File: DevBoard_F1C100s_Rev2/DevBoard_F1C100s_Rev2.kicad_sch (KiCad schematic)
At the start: 59 parts, among them J101 USB_C_Receptacle_USB2.0_16P, J105 UART0, SW105 RESET, SW106 RESET, U101 TPS562201DDCT, U102 TPS562201DDCT, U103 TPS562201DDCT, U104 W25Q16JVSS, U105 F1C100s, Y101 24Mhz

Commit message: WIP schematic
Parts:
- removed C101, C103, C104, C105, C107, C117, C122: 22uf, Capacitor_SMD:C_0603_1608Metric_Pad1.08x0.95mm_HandSolder, symbol Device:C_Small
- removed C102, C106, C118, C120, C121, C123, C124: 0.1uf, Capacitor_SMD:C_0603_1608Metric_Pad1.08x0.95mm_HandSolder, symbol Device:C_Small
- removed F101: TLC-USMD175, symbol Device:Polyfuse_Small
- removed J101: USB_C_Receptacle_USB2.0_16P, Connector_USB:USB_C_Receptacle_HRO_TYPE-C-31-M-12, symbol Connector:USB_C_Receptacle_USB2.0_16P
- removed J105: UART0, Connector_PinHeader_1.00mm:PinHeader_1x04_P1.00mm_Vertical_SMD_Pin1Left, symbol Connector_Generic:Conn_01x04
- removed L101, L102, L103: 2.2uH, Inductor_SMD:L_APV_ANR252012, symbol Device:L_Small
- removed R101, R102, R103, R104, R111: 5.1K, Resistor_SMD:R_0603_1608Metric_Pad0.98x0.95mm_HandSolder, symbol Device:R_Small
- removed R120: 10k, Resistor_SMD:R_0603_1608Metric_Pad0.98x0.95mm_HandSolder, symbol Device:R_Small
- removed SW106: RESET, Button_Switch_SMD:SW_SPST_CK_RS282G05A3, symbol Switch:SW_Push
- removed TP103, TP106, TP107: TestPoint, TestPoint:TestPoint_Pad_D1.0mm, symbol Connector:TestPoint
- removed TP108: TestPoint, TestPoint:TestPoint_Pad_D2.0mm, symbol Connector:TestPoint
- removed U101, U102, U103: TPS562201DDCT, TPS562201DDCT:DDC0006A_N, symbol TPS562201DDCT:TPS562201DDCT
- removed U105: F1C100s, F1C100s:QFN-88_EP_10x10_Pitch0.4mm, symbol F1C100s:F1C100s
- added C? (x2): 0.1uf, Capacitor_SMD:C_0603_1608Metric_Pad1.08x0.95mm_HandSolder, symbol Device:C_Small
- added J?: Micro_SD_Card_Det1, symbol sd_card:Micro_SD_Card_Det1
- added R? (x6): 10k, Resistor_SMD:R_0603_1608Metric_Pad0.98x0.95mm_HandSolder, symbol Device:R_Small
- added SW?: FEL, Button_Switch_SMD:SW_SPST_CK_RS282G05A3, symbol Switch:SW_Push
- added U1: F1C100S, symbol F1C100s:F1C100S
- renumbered C108 to C15, C109 to C16, C110 to C17, C112 to C18, C111 to C19, C113 to C20, C119 to C21, C126 to C22, C125 to C23, C127 to C24, C114 to C25, C128 to C26, C116 to C27, C115 to C28, C129 to C29, C131 to C30, C130 to C31, C132 to C32, R107 to R7, R108 to R8, R115 to R9, SW105 to SW2, U104 to U5, Y101 to Y1
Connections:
- net GND: now also C?.2, C?.2, J?.10 (SHIELD), J?.6 (VSS), SW?.1, U1.74 (TVGND), U1.82 (AGND), U1.89 (GND)
- net HOSCI: now also U1.51 (HOSCI)
- net HOSCO: now also U1.52 (HOSCO)
- net RESET: now also U1.70 (~{RESET})
- net SPI0_CLK: now also U1.59 (PC0/SPI0_CLK/SDC1_CLK)
- net SPI0_CS: now also R?.2, SW?.2, U1.60 (PC1/SPI0_CS/SDC1_CMD)
- net SPI0_MISO: now also U1.61 (PC2/SPI0_MISO/SDC1_D0)
- net SPI0_MOSI: now also U1.62 (PC3/SPI0_MOSI/UART0_TX)
- net SVREF: now also U1.33 (SVREF)
- net USB_N: now also U1.68 (USB_DM)
- net USB_P: now also U1.69 (USB_DP)
- net 1V1 renamed 1.1V
- net 1.1V: now also U1.22 (VCC_CORE), U1.35 (VCC_CORE), U1.71 (VCC_CORE)
- net 2V6 renamed 2.6V
- net 2.6V: now also U1.30 (VCC_DRAM), U1.31 (VCC_DRAM), U1.32 (VCC_DRAM), U1.34 (VCC_DRAM), U1.36 (VCC_DRAM), U1.80 (AVCC)
- net 3V3 renamed 3.3V
- net 3.3V: now also C?.1, C?.1, J?.4 (VDD), R?.1, R?.1, R?.1, R?.1, R?.1, R?.1, U1.20 (VCC_IO), U1.4 (HPVCC), U1.5 (VCC_IO), U1.50 (VCC_IO), U1.67 (USB_VCC), U1.73 (TV_VCC)
- new net LCD_CLK: U1.26 (PD18/LCD_CLK/SPI0_CS)
- new net LCD_D0: U1.49 (PE0/CSI_HSYNC/LCD_D0)
- new net LCD_D1: U1.48 (PE1/CSI_VSYNC/LCD_D1)
- new net LCD_D10: U1.12 (PD6/LCD_D10/TWI1_SDA)
- new net LCD_D11: U1.13 (PD7/LCD_D11/DA_MCLK)
- new net LCD_D12: U1.14 (PD8/LCD_D12/DA_BCLK)
- new net LCD_D13: U1.15 (PD9/LCD_D13/DA_LRCK)
- new net LCD_D14: U1.16 (PD10/LCD_D14/DA_IN)
- new net LCD_D15: U1.17 (PD11/LCD_D15/DA_OUT)
- new net LCD_D16: U1.45 (PE4/CSI_D1/LCD_D16)
- new net LCD_D17: U1.44 (PE5/CSI_D2/LCD_D17)
- new net LCD_D18: U1.18 (PD12/LCD_D18/TWI0_SCK)
- new net LCD_D19: U1.19 (PD13/LCD_D19/UART2_TX)
- new net LCD_D2: U1.6 (PD0/LCD_D2/TWI0_SDA)
- new net LCD_D20: U1.21 (PD14/LCD_D20/UART2_RX)
- new net LCD_D21: U1.23 (PD15/LCD_D21/UART2_RTS)
- new net LCD_D22: U1.24 (PD16/LCD_D22/UART2_CTS)
- new net LCD_D23: U1.25 (PD17/LCD_D23/OWA_OUT)
- new net LCD_D3: U1.7 (PD1/LCD_D3/UART1_RTS)
- new net LCD_D4: U1.8 (PD2/LCD_D4/UART1_CTS)
- new net LCD_D5: U1.9 (PD3/LCD_D5/UART1_RX)
- new net LCD_D6: U1.10 (PD4/LCD_D6/UART1_TX)
- new net LCD_D7: U1.11 (PD5/LCD_D7/TWI1_SCK)
- new net LCD_D8: U1.47 (PE2/CSI_PCLK/LCD_D8)
- new net LCD_D9: U1.46 (PE3/CSI_D0/LCD_D9)
- new net LCD_DE: U1.27 (PD19/LCD_DE/SPI0_MOSI)
- new net LCD_HSYNC: U1.28 (PD20/LCD_HSYNC/SPI0_CLK)
- new net LCD_VSYNC: U1.29 (PD21/LCD_VSYNC/SPI0_MISO)
- new net SDC0_CLK: J?.5 (CLK), U1.56 (PF2/SDC0_CLK/UART0_RX)
- new net SDC0_CMD: J?.3 (CMD), R?.2, U1.55 (PF3/SDC0_CMD/DBG_DO)
- new net SDC0_D0: J?.7 (DAT0), R?.2, U1.57 (PF1/SDC0_D0/DBG_DI)
- new net SDC0_D1: J?.8 (DAT1), R?.2, U1.58 (PF0/SDC0_D1/DBG_MS)
- new net SDC0_D2: J?.1 (DAT2), R?.2, U1.53 (PF5/SDC0_D2/DBG_CK)
- new net SDC0_D3: J?.2 (DAT3/CD), R?.2, U1.54 (PF4/SDC0_D3/UART0_TX)
- no-connect marks 66 -> 28
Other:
- added sheet Power (./sheets/power.kicad_sch)
- note added: "Power 1.1V: VCORE 2.6V: AVCC, VCC_DRAM 3.3V: VCC_IO, USB_VCC, TV_AVCC, HP_VCC"
- note removed: "Power VCORE: 1.1V 2A VIO: 3.3V 1A VDRAM: 2.6V 1A"
- moved on the sheet: C15, C16, C17, C18, C19, C20, C21, C22, C23, C24, C25, C26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

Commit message: Finish schematic rev2
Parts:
- added C101: 0.1uf, Capacitor_SMD:C_0603_1608Metric_Pad1.08x0.95mm_HandSolder, symbol Device:C_Small
- added J101: LCD_40pin_FPC, symbol lcd_rgb_fpc:40pin_24bit
- added R101: 10k, Resistor_SMD:R_0603_1608Metric_Pad0.98x0.95mm_HandSolder, symbol Device:R_Small
- added SW101: RESET, Button_Switch_SMD:SW_SPST_CK_RS282G05A3, symbol Switch:SW_Push
- added TP101, TP102: TestPoint, TestPoint:TestPoint_Pad_D1.0mm, symbol Connector:TestPoint
- added TP103: TestPoint, TestPoint:TestPoint_Pad_D2.0mm, symbol Connector:TestPoint
- R7, R8: value 5.1K -> 2.2k
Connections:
- net 3.3V: now also J101.4 (VCC), R101.1
- net GND: now also C101.2, J101.29 (GND), J101.3 (GND), J101.36 (GND), SW101.1; no longer C16.1, Y1.2
- net LCD_CLK: now also J101.30 (PCLK)
- net LCD_D0: now also J101.21 (B0)
- net LCD_D1: now also J101.22 (B1)
- net LCD_D10: now also J101.15 (G2)
- net LCD_D11: now also J101.16 (G3)
- net LCD_D12: now also J101.17 (G4)
- net LCD_D13: now also J101.18 (G5)
- net LCD_D14: now also J101.19 (G6)
- net LCD_D15: now also J101.20 (G7)
- net LCD_D16: now also J101.5 (R0)
- net LCD_D17: now also J101.6 (R1)
- net LCD_D18: now also J101.7 (R2)
- net LCD_D19: now also J101.8 (R3)
- net LCD_D2: now also J101.23 (B2)
- net LCD_D20: now also J101.9 (R4)
- net LCD_D21: now also J101.10 (R5)
- net LCD_D22: now also J101.11 (R6)
- net LCD_D23: now also J101.12 (R7)
- net LCD_D3: now also J101.24 (B3)
- net LCD_D4: now also J101.25 (B4)
- net LCD_D5: now also J101.26 (B5)
- net LCD_D6: now also J101.27 (B6)
- net LCD_D7: now also J101.28 (B7)
- net LCD_D8: now also J101.13 (G0)
- net LCD_D9: now also J101.14 (G1)
- net LCD_DE: now also J101.34 (DEN)
- net LCD_HSYNC: now also J101.32 (HSYNC)
- net LCD_VSYNC: now also J101.33 (VSYNC)
- net SPI1_MISO: now reaches U1.39 (PE10/CSI_D7/UART2_CTS/SPI1_MISO)
- net SPI1_MISO: now also J101.31 (SDO)
- net SPI1_CLK: now reaches U1.40 (PE9/CSI_D6/UART2_RTS/SPI1_CLK)
- net SPI1_CLK: now also J101.39 (SCL)
- net SPI1_MOSI: now reaches U1.41 (PE8/CSI_D5/UART2_RX/SPI1_MOSI)
- net SPI1_MOSI: now also J101.38 (SDA)
- net SPI1_CS: now reaches U1.42 (PE7/CSI_D4/UART2_TX/SPI1_CS)
- net SPI1_CS: now also J101.40 (CS)
- net PWM1: now reaches U1.43 (PE6/CSI_D3/PWM1)
- net PWM1: now also TP101.1
- net PWM0: now reaches U1.64 (PA2/TPY1/PWM0)
- net PWM0: now also TP102.1
- net LRADC0: now reaches U1.79 (LRADC0)
- net LRADC0: now also TP103.1
- net RESET: no longer names the net of C27.1, R9.2, SW2.2, U1.70 (~{RESET})
- net SVREF: no longer names the net of R7.2, R8.1, U1.33 (SVREF)
- new net: C16.1, Y1.2
- new net LCD_RESET: C101.1, J101.37 (RESET), R101.2, SW101.2
- new net VLEDA: J101.2 (LEDA)
- new net VLEDK: J101.1 (LEDK)
- no-connect marks 28 -> 22
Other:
- note added: "F1C100s SIP"
- note added: "Flash"
- note added: "LCD"
- note added: "Micro SD card"
- note added: "Power"
- moved on the sheet: C15, C16, C17, C18, C19, C20, C21, C22, C23, C24, C25, C26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

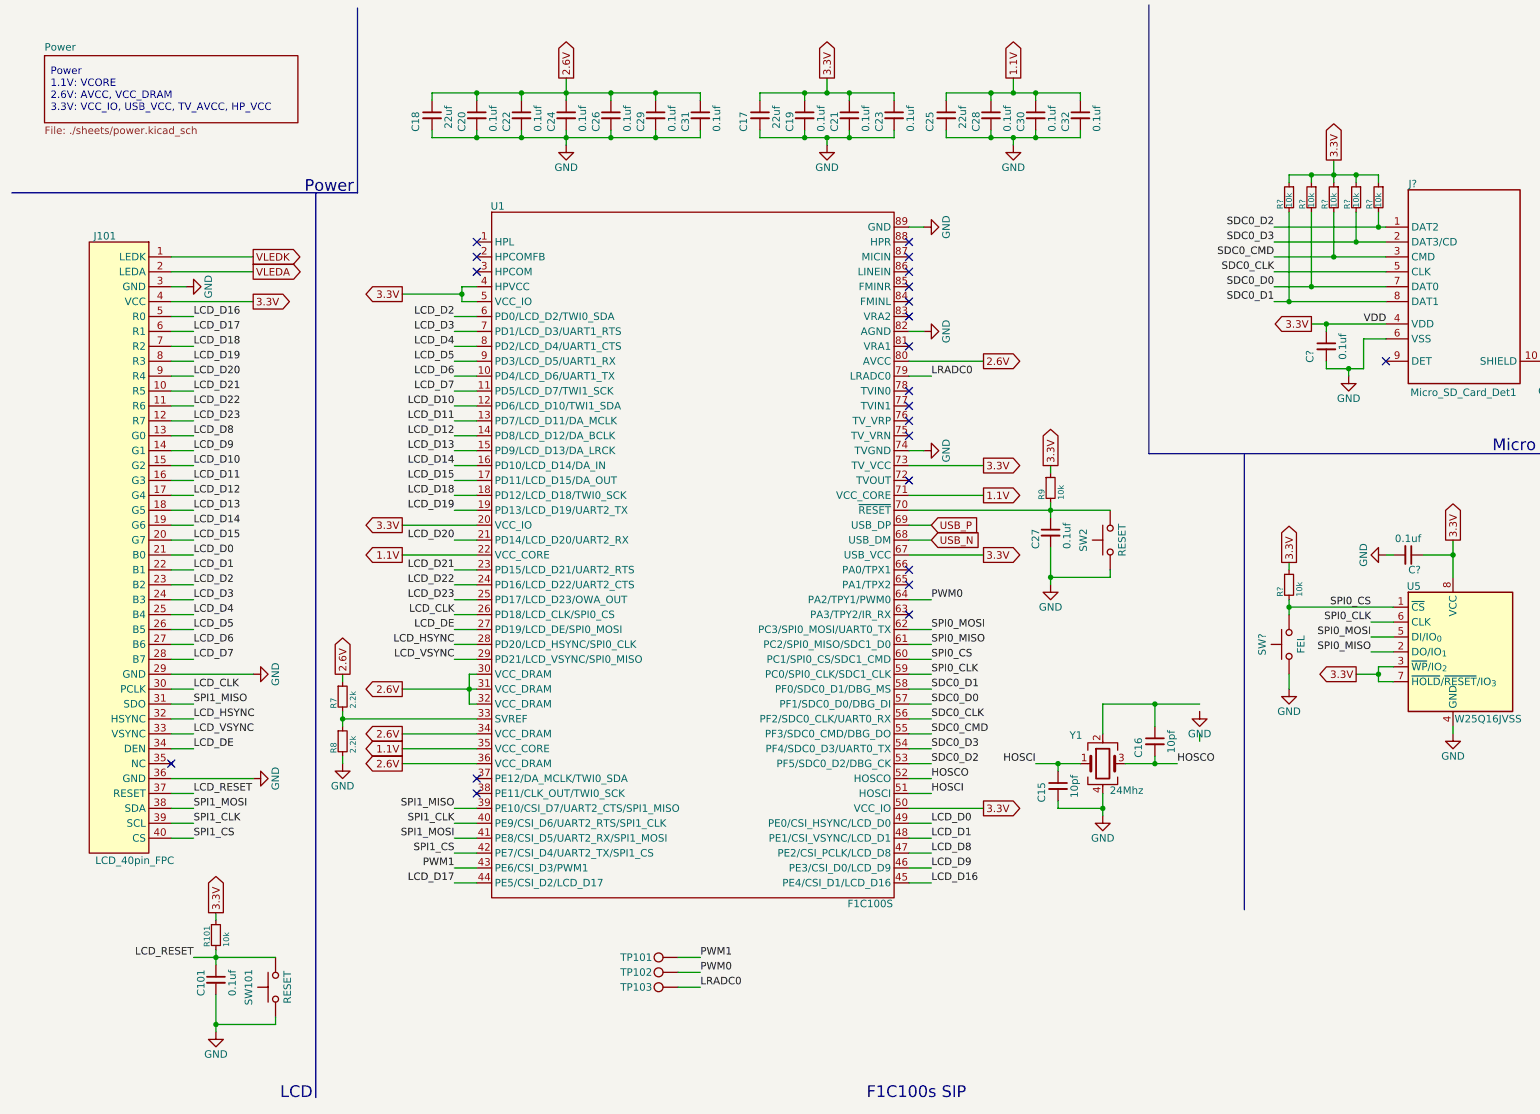
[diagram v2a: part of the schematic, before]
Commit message: Update schematic annotations
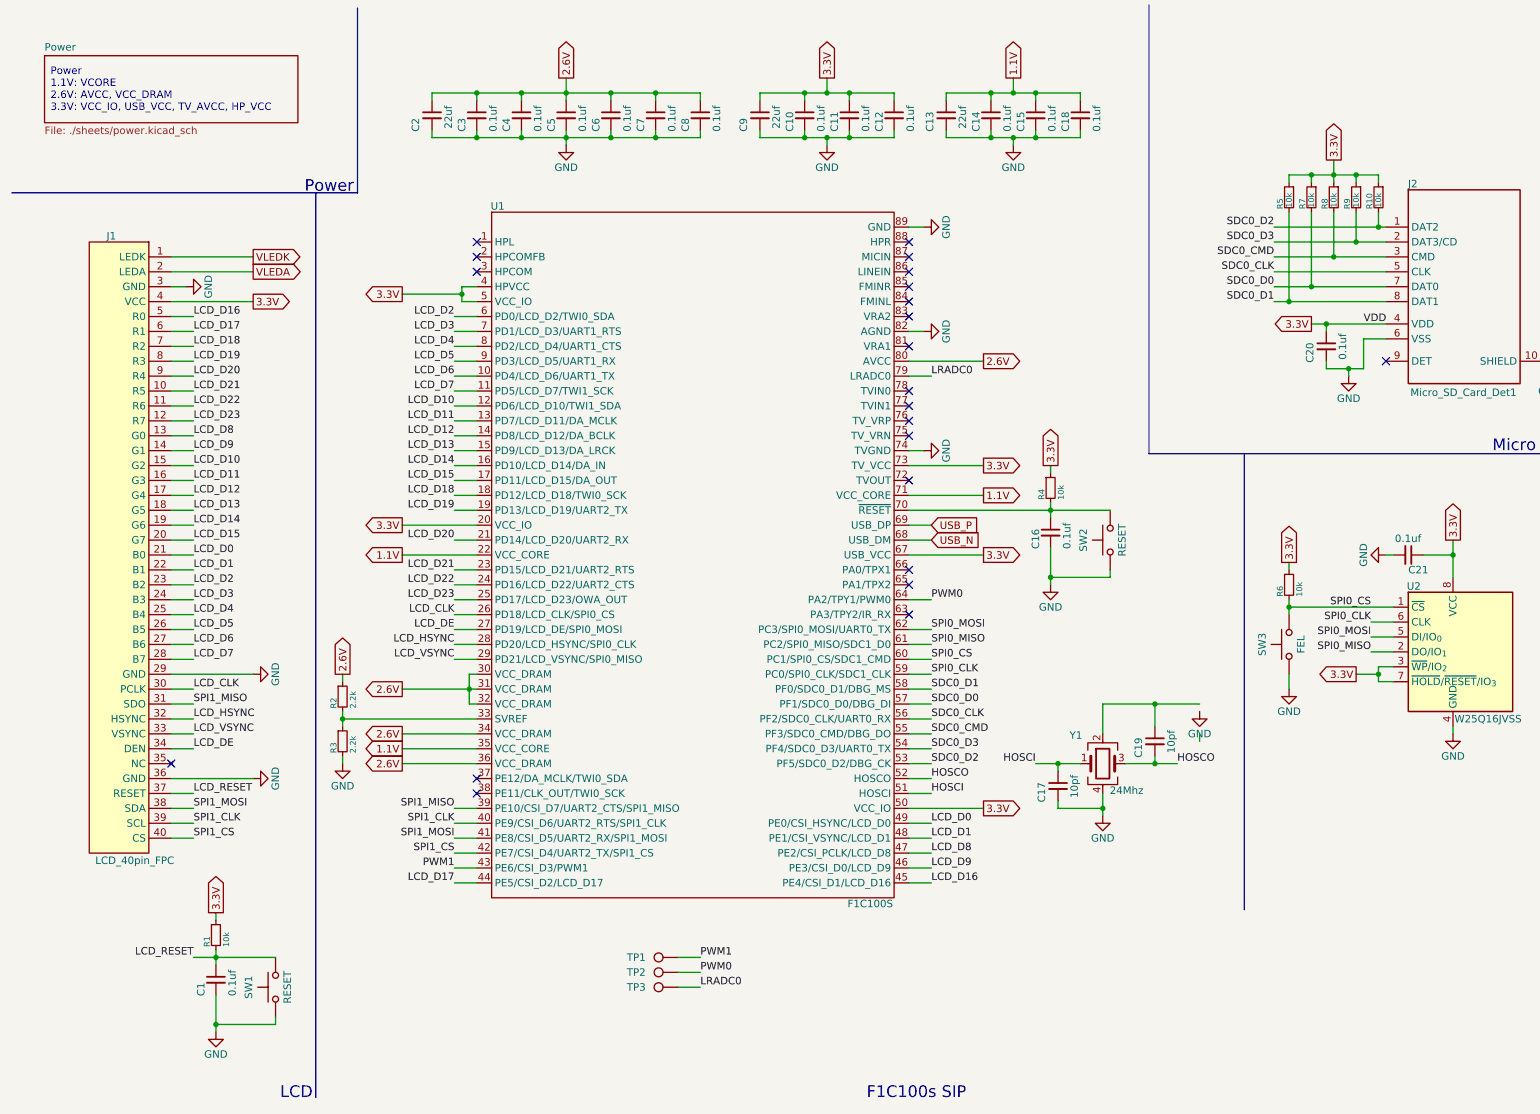
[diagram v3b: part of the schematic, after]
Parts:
- J1: renamed from J101; footprint (none) -> lcd_rgb_fpc:40pin_0.5mm_Vertical
- J2: renamed from J?; footprint (none) -> sd_card:sd_card_10p
- U1: footprint (none) -> F1C100s:QFN-88_EP_10x10_Pitch0.4mm
- gave numbers to parts that had none: 9
- renumbered C101 to C1, C19 to C10, C21 to C11, C23 to C12, C25 to C13, C28 to C14, C30 to C15, C27 to C16, C15 to C17, C32 to C18, C16 to C19, C18 to C2, C20 to C3, C22 to C4, C24 to C5, C26 to C6, C29 to C7, C31 to C8, C17 to C9, R101 to R1, R7 to R2, R8 to R3, R9 to R4, SW101 to SW1, TP101 to TP1, TP102 to TP2, TP103 to TP3, U5 to U2

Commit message: Update schematic and footprints
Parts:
- TP3: footprint TestPoint:TestPoint_Pad_D2.0mm -> TestPoint:TestPoint_Pad_D1.0mm
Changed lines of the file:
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@@
 			)
 		)
-		(property "Footprint" "TestPoint:TestPoint_Pad_D2.0mm"
+		(property "Footprint" "TestPoint:TestPoint_Pad_D1.0mm"
 			(at 125.73 173.99 0)
 			(effects

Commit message: Finish layout
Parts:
- removed C1: 0.1uf, Capacitor_SMD:C_0603_1608Metric_Pad1.08x0.95mm_HandSolder, symbol Device:C_Small
- removed SW1: RESET, Button_Switch_SMD:SW_SPST_CK_RS282G05A3, symbol Switch:SW_Push
- SW3: value FEL -> BOOT
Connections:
- net GND: now also C19.1, Y1.2
- net LCD_RESET: no longer names the net of J1.37 (RESET), R1.2
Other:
- moved on the sheet: R1
